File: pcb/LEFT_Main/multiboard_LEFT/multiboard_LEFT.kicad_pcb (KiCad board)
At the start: 2 copper layers, 235.3 x 146.2 mm, 111 parts, among them SW1 RotaryEncoder_Switch, SW10 SW_Push, SW11 SW_Push, SW12 SW_Push, SW13 SW_Push, SW14 SW_Push, SW15 SW_Push, SW16 SW_Push, SW17 SW_Push, SW18 SW_Push, SW19 SW_Push, SW2 RotaryEncoder_Switch, SW20 SW_Push, SW21 SW_Push, SW22 SW_Push, SW23 SW_Push, SW24 SW_Push, SW25 SW_Push, SW26 SW_Push, SW27 SW_Push, SW28 SW_Push, SW29 SW_Push, SW3 SW_Push, SW30 SW_Push, SW31 SW_Push, SW32 SW_Push, SW33 SW_Push, SW34 SW_Push, SW35 SW_Push, SW36 SW_Push, SW37 SW_Push, SW38 SW_Push, SW39 SW_Push, SW4 SW_Push, SW40 SW_Push, SW41 SW_Push, SW42 SW_Push, SW46 SW_Push, SW47 SW_Push, SW48 SW_Push, SW49 SW_Push, SW5 SW_Push, SW50 SW_Push, SW51 SW_Push, SW52 SW_Push, SW56 SW_Push, SW57 SW_Push, SW58 SW_Push, SW59 SW_Push, SW6 SW_Push, SW60 SW_Push, SW61 SW_Push, SW62 SW_Push, SW7 SW_Push, SW8 SW_Push, SW9 SW_Push, U1 ESP32-S3-DEVKITC-1-N8R2

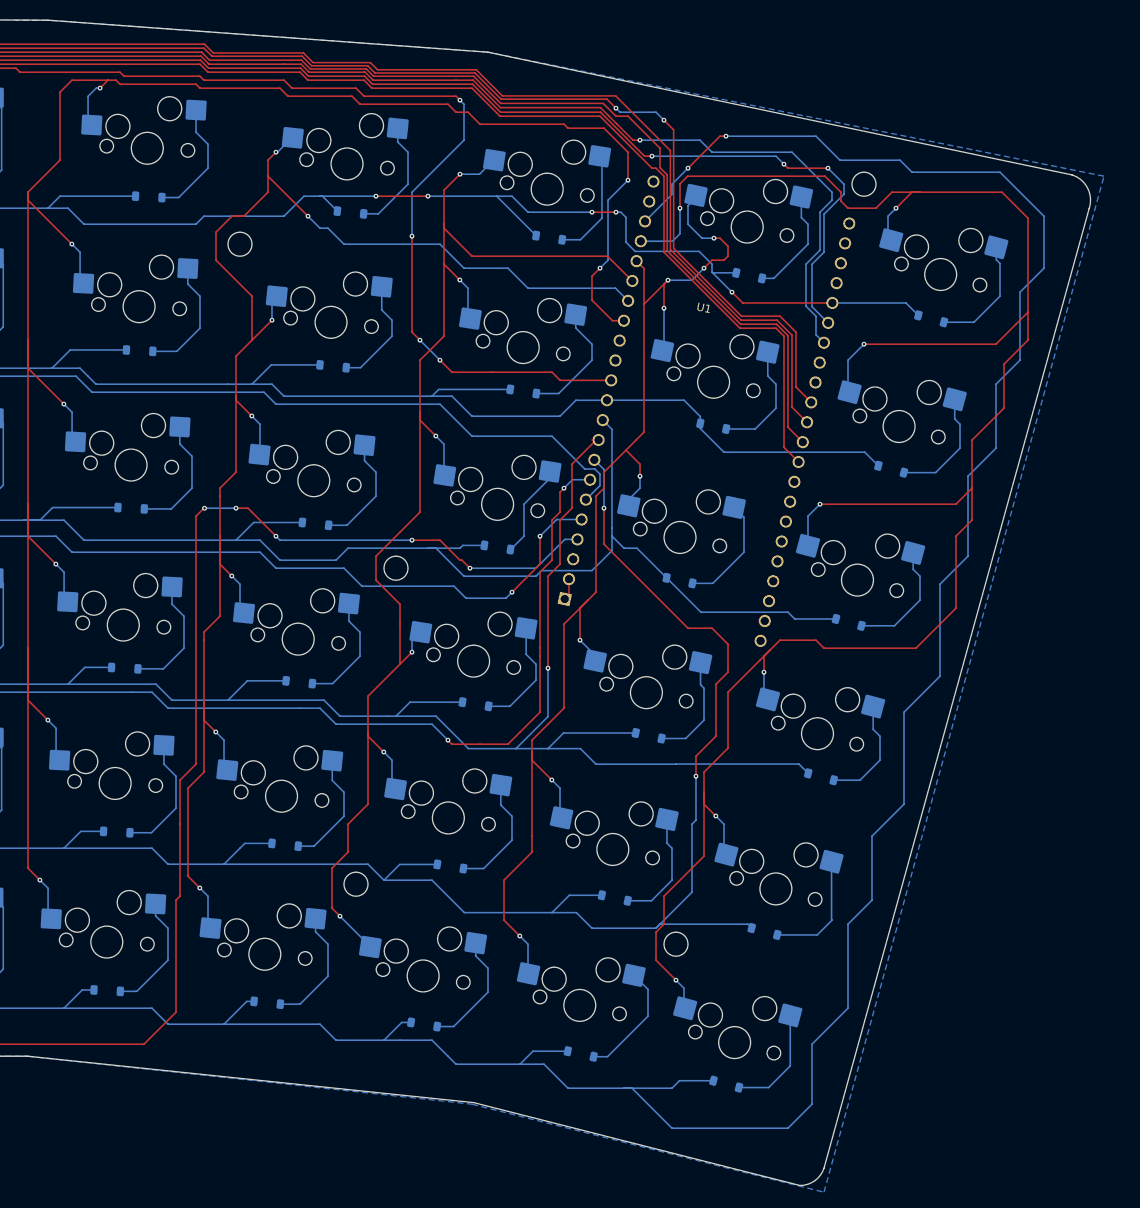
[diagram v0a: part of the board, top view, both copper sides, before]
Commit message: add headphone jack
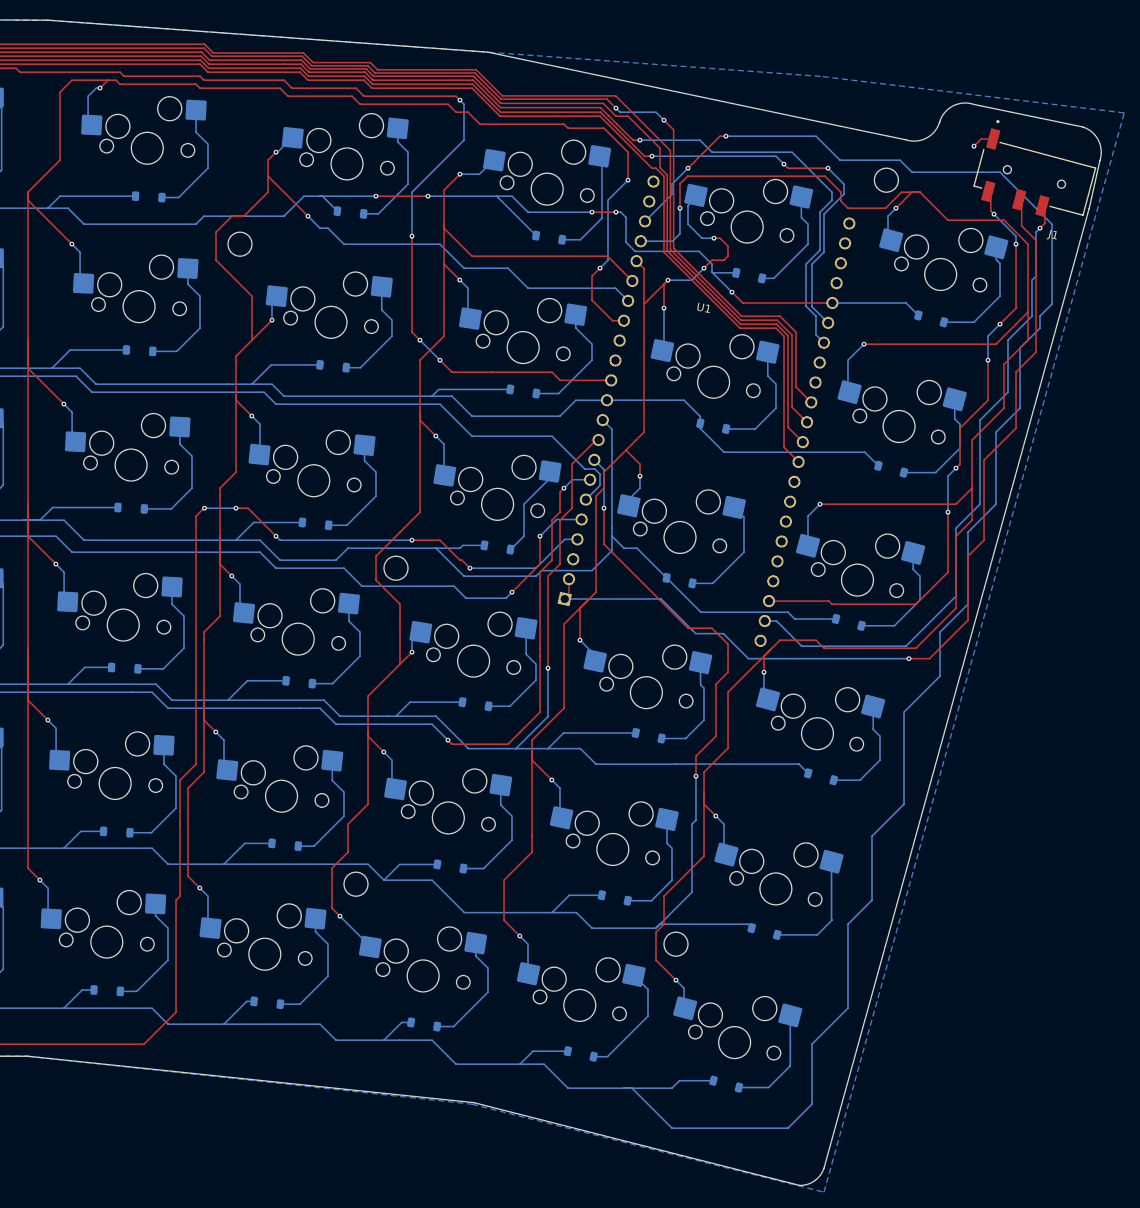
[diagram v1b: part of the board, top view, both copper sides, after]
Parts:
- added J1: PJ-320D-A, PJ:HRO_PJ-320D-A, F.Cu at (270.3, 34.1)
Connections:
- net Net-(U1-3V3-PadJ1_1) renamed +3.3V
- U1 pad J3_2: unconnected-(U1-U0TXD/GPIO43-PadJ3_2) -> TX
- U1 pad J3_3: unconnected-(U1-U0RXD/GPIO44-PadJ3_3) -> RX
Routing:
- net +3.3V: track 2.70 -> 115.0 mm, vias 0 -> 1
- net TX: track 0.00 -> 81.2 mm, vias 0 -> 1
- net RX: track 0.00 -> 76.6 mm, vias 0 -> 6
- net GND: track 0.00 -> 3.09 mm, vias 0 -> 1
- net ROW10: track 268.2 -> 266.3 mm
- net COL4: track 280.9 -> 279.9 mm
- net COL1: track 436.0 -> 436.9 mm
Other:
- board size 235.3 x 146.2 mm -> 236.7 x 146.2 mm
